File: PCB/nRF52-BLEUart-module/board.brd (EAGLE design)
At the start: 40 x 16 mm, 2 parts, among them J1 USB-A_PTH_MALE, U1 NRF52832

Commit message: PCB update
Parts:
- added C1: 0402, angrypig7-RCL:C0402
- added C10: 2.2uF, angrypig7-RCL:C0603
- added C11, C13, C14, C15, C4, C6: 100nF, angrypig7-RCL:C0402
- added C12: 4.7uF, angrypig7-RCL:C0402
- added C16, C17, C7, C8: 12pF, angrypig7-RCL:C0402
- added C2: 0603, angrypig7-RCL:C0603
- added C3: 0805, angrypig7-RCL:C0805
- added C5: 10uF, angrypig7-RCL:C0603
- added C9: 1uF, angrypig7-RCL:C0402
- added D1: B5819W, angrypig7-Diodes:SOD-123
- added JP1: (no value), angrypig7-Connectors-PinHeads:1X04
- added TC1: TC2030-IDC-NL, angrypig7-Connectors-Programming:TC2030-IDC-NL
- added TP1: TEST-POINT-3, angrypig7-Tests:PAD-3X-RECT-SILK
- added VR1: AP2210K-3.3TRG, angrypig7-IC-Power:SOT-23-5
- added Y1: 32.768kHz, angrypig7-Clocks:CRYSTAL-SMD-3.2X1.5MM
- added Y2: 32MHz_2016, angrypig7-Clocks:CRYSTAL-SMD-2.0X1.6MM
- moved U1 17.7 mm to (37.7, 9.65)
- moved J1 1.28 mm to (3.17, 9.27)
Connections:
- removed net VBUS: J1.VBUS
- new net 3V3: C10.1, C12.1, C14.1, C15.1, TC1.1, TP1.P$2, U1.13, U1.36, U1.48, VR1.5
- new net 5V: C9.1, D1.C, TP1.P$3, VR1.1, VR1.3
- new net N$1: C8.2, U1.2, Y1.P$2
- new net N$2: C4.1, D1.A, J1.VBUS
- new net N$3: C6.1, VR1.4
- new net N$4: C7.2, U1.3, Y1.P$1
- new net N$5: C11.1, U1.1
- new net N$6: U1.30
- new net N$7: C13.1, U1.46
- new net N$8: C17.1, U1.35, Y2.3
- new net N$9: C16.1, U1.34, Y2.1
- new net NRST: TC1.3, U1.24
- new net SWDCLK: TC1.4, U1.25
- new net SWDIO: TC1.2, U1.26
- new net SWO: TC1.6, U1.21
- new net USB_D_N: J1.D-
- new net USB_D_P: J1.D+
- net GND: now also C10.2, C11.2, C12.2, C13.2, C14.2, C15.2, C16.2, C17.2, C4.2, C6.2, C7.1, C8.1, C9.2, J1.SHIELD@0, J1.SHIELD@1, J1.SHIELD@2, J1.SHIELD@3, TC1.5, TP1.P$1, U1.45, VR1.2, Y2.2, Y2.4
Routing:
- added copper zone on layer 1, net GND
- added copper zone on layer 16, net GND
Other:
- board size 40 x 16 mm -> 55 x 18 mm

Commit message: PCB update
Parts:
- added D2: TVS, angrypig7-Diodes:SPT-23-6
- added D3, D4, D5, D6: 0603, angrypig7-Diodes:LED_0603
- added L1: (no value), angrypig7-RCL:R0402
- added R1, R2, R3, R4, R5: 10k, angrypig7-RCL:R0402
- added S1: SPST-3x4mm, angrypig7-Switches:TACTILE_SWITCH_SMD_3.0X4.0MM
- added U2: NRF52832, angrypig7-IC-MCU:QFN40P600X600X90-49T450N
- C1: value 0402 -> 1uF
- C10: value 2.2uF -> 100nF; device angrypig7-RCL:C0603 -> angrypig7-RCL:C0402
- C11, C6: value 100nF -> 12pF
- C12: value 4.7uF -> 100nF
- C13: value 100nF -> 100pF
- C14: value 100nF -> 1uF
- C15: value 100nF -> 0.8pF
- C16: value 12pF -> 0.8pF
- C17: value 12pF -> 100nF
- C2: value 0603 -> 2.2uF
- C3: value 0805 -> 100nF; device angrypig7-RCL:C0805 -> angrypig7-RCL:C0402
- C5: value 10uF -> 4.7uF; device angrypig7-RCL:C0603 -> angrypig7-RCL:C0402
- C9: value 1uF -> 100nF
- JP1: value (none) -> V G Rx Tx; device angrypig7-Connectors-PinHeads:1X04 -> angrypig7-Connectors-PinHeads:1X04/90
- U1: value NRF52832 -> CH340E; device angrypig7-IC-MCU:QFN40P600X600X90-49T450N -> angrypig7-IC:MSOP-10
- Y1: value 32.768kHz -> 32MHz_2016; device angrypig7-Clocks:CRYSTAL-SMD-3.2X1.5MM -> angrypig7-Clocks:CRYSTAL-SMD-2.0X1.6MM
- Y2: value 32MHz_2016 -> 32.768kHz; device angrypig7-Clocks:CRYSTAL-SMD-2.0X1.6MM -> angrypig7-Clocks:CRYSTAL-SMD-3.2X1.5MM
- moved C12 29.6 mm to (7.75, 2.03)
- moved U1 28.3 mm to (10.0, 3.68), turned to 270 degrees
- moved Y2 22.6 mm to (21.3, 11.4)
- moved C17 22.2 mm to (24.4, 4.57), turned to 180 degrees
- moved C6 21.7 mm to (32.4, 14.1), turned to 0 degrees
- moved C4 21.2 mm to (25.8, 13.0), turned to 0 degrees
- moved C9 17.2 mm to (30.2, 13.0), turned to 90 degrees
- moved C14 13.5 mm to (27.2, -5.46), turned to 0 degrees
- moved TC1 13.0 mm to (30.9, 2.54), turned to 180 degrees
- moved C1 12.7 mm to (15.4, 16.9), turned to 180 degrees
- moved C2 12.0 mm to (14.9, 11.2), turned to 180 degrees
- moved C5 11.4 mm to (24.1, 13.2)
- moved C15 11.1 mm to (31.9, 7.37), turned to 270 degrees
- moved C7 10.2 mm to (19.6, 10.3)
- moved C8 10.2 mm to (19.6, 12.6)
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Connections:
- removed net USB_D_N: J1.D-
- removed net USB_D_P: J1.D+
- new net N$10: C13.1, U2.33
- new net N$11: U2.32
- new net N$12: D4.A, R3.1
- new net N$13: D5.A, R4.1
- new net N$14: D6.A, R5.1
- new net RF-1: C15.1, L1.1, U2.30
- new net RF-2: C16.1, L1.2
- new net UART_RX: JP1.4, U1.9
- new net UART_TX: JP1.3, U1.8
- new net USB_N: D2.4, D2.6, J1.D-, U1.2
- new net USB_P: D2.1, D2.3, J1.D+, U1.1
- net 3V3: now also C17.1, C2.1, C5.1, C9.1, JP1.1, R1.2, R2.2, R3.2, R4.2, R5.2, U1.10, U1.7, U2.13, U2.36, U2.48; no longer C10.1, C14.1, C15.1, U1.13, U1.36, U1.48
- net 5V: now also C1.1; no longer C9.1
- net GND: now also C1.2, C2.2, C3.2, C5.2, D2.2, D3.C, JP1.2, S1.1, U1.3, U2.31, U2.45, U2.49, Y1.2, Y1.4; no longer U1.45, Y2.2, Y2.4
- net N$1: now also U2.2, Y2.P$2; no longer U1.2, Y1.P$2
- net N$2: now also D2.5; no longer C4.1
- net N$3: now also C3.1; no longer C6.1
- net N$4: now also U2.3, Y2.P$1; no longer U1.3, Y1.P$1
- net N$5: now also C10.1, U2.1; no longer C11.1, U1.1
- net N$6: now also D3.A, R1.1; no longer U1.30
- net N$7: now also C4.1, U2.46; no longer C13.1, U1.46
- net N$8: now also C6.1, U2.35, Y1.3; no longer C17.1, U1.35, Y2.3
- net N$9: now also C11.1, U2.34, Y1.1; no longer C16.1, U1.34, Y2.1
- net NRST: now also C14.1, R2.1, S1.2, U2.24; no longer U1.24
- net SWDCLK: now also U2.25; no longer U1.25
- net SWDIO: now also U2.26; no longer U1.26
- net SWO: now also U2.21; no longer U1.21
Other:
- board size 55 x 18 mm -> 50 x 18 mm

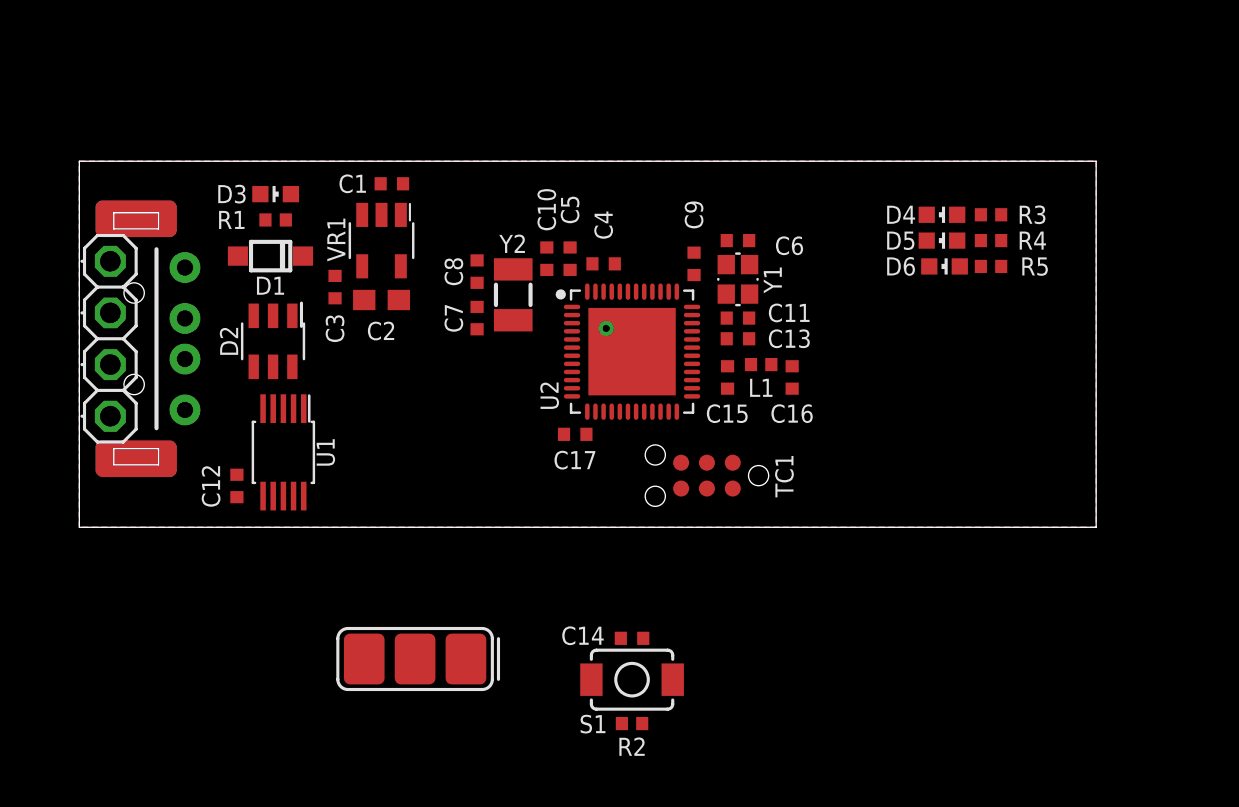
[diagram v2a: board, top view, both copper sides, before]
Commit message: PCB update with inverted F antenna
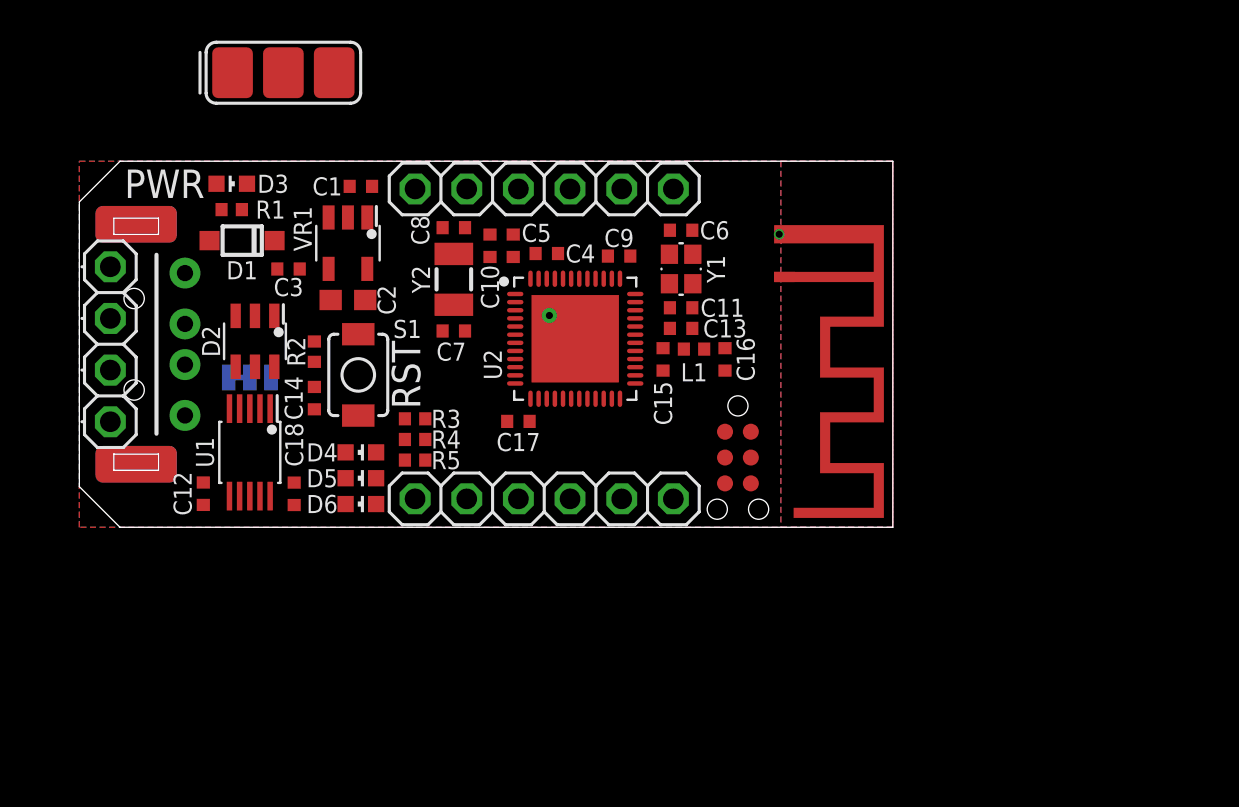
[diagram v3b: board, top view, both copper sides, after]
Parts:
- added C18: 100nF, angrypig7-RCL:C0402
- added JP2: 5V 3V3, angrypig7-Jumpers:SMT-JUMPER_3_1-NC_TRACE_NO-SILK
- added JP3, JP4: (no value), angrypig7-Connectors-PinHeads:1X06
- added U$1: INVERTED_F_2.4GHZ_TI-AN043_L, angrypig7-Antennas:TI-AN043_LEFT
- C15, C16: value 0.8pF -> (none)
- D3: value 0603 -> PWR
- L1: value (none) -> 0R
- moved D6 31.0 mm to (13.8, 1.14)
- moved D4 30.9 mm to (13.8, 3.68)
- moved D5 30.9 mm to (13.8, 2.41)
- moved R3 30.0 mm to (16.5, 5.33)
- moved R4 30.0 mm to (16.5, 4.32)
- moved R5 29.9 mm to (16.5, 3.30)
- moved TP1 29.5 mm to (10.0, 22.4), turned to 0 degrees
- moved R2 24.1 mm to (11.6, 8.64), turned to 90 degrees
- moved S1 20.1 mm to (13.7, 7.49), turned to 270 degrees
- moved C14 19.6 mm to (11.6, 6.35), turned to 270 degrees
- moved C9 3.70 mm to (26.5, 13.3), turned to 180 degrees
- moved C16 3.42 mm to (31.8, 8.26)
- moved L1 3.39 mm to (30.2, 8.76)
- moved C15 3.30 mm to (28.7, 8.26)
- moved Y2 3.02 mm to (18.4, 12.2)
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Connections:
- new net N$15: C12.1, JP2.2, U1.7
- new net N$16: C18.1, U1.10
- net 3V3: now also JP2.3; no longer C12.1, U1.10, U1.7
- net 5V: now also JP2.1
- net GND: now also C18.2, U$1.GND
- net RF-2: now also U$1.RF
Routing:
- added copper zone on layer 1, net GND-CUTOUT
- added copper zone on layer 16, net GND-CUTOUT2
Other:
- board size 50 x 18 mm -> 40 x 18 mm
- board text added: "RST"

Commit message: artwork partially done, layout update
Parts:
- added C19: TP, angrypig7-RCL:C0603
- JP1: value V G Rx Tx -> V G Tx Rx
- JP3, JP4: device angrypig7-Connectors-PinHeads:1X06 -> angrypig7-Connectors-PinHeads:1X05-NOSILK
- moved TP1 6.26 mm to (10.7, 16.1), flipped to the bottom
- moved JP2 5.68 mm to (10.9, 12.4), turned to 270 degrees
- moved C11 3.95 mm to (31.8, 14.1), turned to 270 degrees
- moved C16 3.91 mm to (30.9, 12.1), turned to 180 degrees
- moved C15 3.27 mm to (31.9, 9.02), turned to 0 degrees
- moved TC1 2.17 mm to (30.2, 3.17)
- moved L1 2.11 mm to (31.4, 10.5), turned to 90 degrees
- moved C6 1.73 mm to (27.9, 14.1), turned to 90 degrees
- moved Y1 1.42 mm to (29.8, 14.1), turned to 180 degrees
- moved JP1 1.40 mm to (2.92, 9.00)
- moved JP4 1.29 mm to (21.6, 1.20)
- moved JP3 1.28 mm to (21.6, 16.8)
- moved C13 1.09 mm to (29.2, 10.8), turned to 90 degrees
- moved U$1 0.88 mm to (33.3, 14.7)
- moved C9 0.85 mm to (26.9, 14.1), turned to 90 degrees
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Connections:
- net N$2 renamed USB_IN
- removed net N$15: C12.1, JP2.2, U1.7
- new net VCCIO: C12.1, JP1.1, JP2.2, U1.7
- net 3V3: no longer JP1.1
- net GND: now also C19.2
- net RF-1: now also C19.1
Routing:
- net VCCIO: track 0.00 -> 23.1 mm, vias 0 -> 1
- net 3V3: track 0.00 -> 22.9 mm, vias 0 -> 3
- net UART_RX: track 0.00 -> 15.5 mm, vias 0 -> 1
- net 5V: track 0.00 -> 13.2 mm, vias 0 -> 1
- net USB_IN: track 0.00 -> 12.2 mm, vias 0 -> 2
- net UART_TX: track 0.00 -> 12.0 mm, vias 0 -> 2
- net USB_P: track 0.00 -> 11.3 mm
- net USB_N: track 0.00 -> 8.85 mm
- net N$1: track 0.00 -> 5.36 mm
- net N$4: track 0.00 -> 4.58 mm
- net NRST: track 0.00 -> 4.10 mm
- net N$5: track 0.00 -> 2.63 mm
- net N$16: track 0.00 -> 1.71 mm
- net N$3: track 0.00 -> 1.58 mm
- net N$7: track 0.00 -> 1.47 mm
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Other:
- board size 40 x 18 mm -> 39 x 18 mm

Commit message: finished PCB artwork
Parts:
- removed C19: TP, angrypig7-RCL:C0603
- JP2: value 5V 3V3 -> 3V3 5V
- U$1: value INVERTED_F_2.4GHZ_TI-AN043_L -> ANT
- moved TC1 1.14 mm to (30.7, 4.19)
- moved C13 0.38 mm to (29.2, 10.4)
- moved C15 0.38 mm to (31.5, 9.02)
- moved L1 0.38 mm to (31.0, 10.5)
- moved C16 0.25 mm to (30.6, 12.1)
- moved D4 0.18 mm to (13.8, 3.94)
- moved D5 0.18 mm to (13.8, 2.67)
- moved D6 0.18 mm to (13.8, 1.40)
- moved C7 0.13 mm to (18.3, 9.27), turned to 0 degrees
- moved C8 0.13 mm to (18.3, 14.4), turned to 0 degrees
- moved Y2 0.13 mm to (18.3, 11.8)
- turned JP2 to 90 degrees
- turned R3 to 180 degrees
- turned R4 to 180 degrees
- turned R5 to 180 degrees
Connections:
- removed net N$13: D5.A, R4.1
- new net LED1: R3.1, U2.17
- new net LED2: R4.1, U2.18
- new net LED3: R5.1, U2.19
- new net N$2: D4.A, R3.2
- new net P0.02: JP4.2, U2.4
- new net P0.03: JP4.3, U2.5
- new net P0.04: JP4.4, U2.6
- new net P0.05: JP4.5, U2.7
- new net P0.28: JP3.5, U2.40
- new net P0.29: JP3.4, U2.41
- new net P0.30: JP3.3, U2.42
- new net P0.31: JP3.2, U2.43
- net 3V3: now also JP2.1, JP3.1; no longer JP2.3, R3.2, R4.2, R5.2
- net 5V: now also JP2.3; no longer JP2.1
- net GND: now also D4.C, D5.C, D6.C, JP4.1; no longer C19.2
- net N$12: now also D5.A, R4.2; no longer D4.A, R3.1
- net N$14: now also R5.2; no longer R5.1
- net RF-1: no longer C19.1
- net UART_RX: now also U1.8, U2.10; no longer U1.9
- net UART_TX: now also U1.9, U2.8; no longer U1.8
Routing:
- net 3V3: track 22.9 -> 64.2 mm, vias 3 -> 8
- net NRST: track 4.10 -> 24.7 mm, vias 0 -> 2
- net UART_TX: track 12.0 -> 28.3 mm, vias 2 -> 4
- net UART_RX: track 15.5 -> 29.8 mm, vias 1 -> 3
- net P0.05: track 0.00 -> 14.1 mm
- net P0.04: track 0.00 -> 12.7 mm
- net LED3: track 0.00 -> 12.3 mm, vias 0 -> 2
- net LED2: track 0.00 -> 11.6 mm, vias 0 -> 2
- net P0.03: track 0.00 -> 11.4 mm
- net P0.02: track 0.00 -> 11.1 mm
- net LED1: track 0.00 -> 11.1 mm, vias 0 -> 2
- net P0.31: track 0.00 -> 8.80 mm
- net SWO: track 0.00 -> 8.41 mm, vias 0 -> 2
- net N$9: track 0.00 -> 7.32 mm
- net P0.30: track 0.00 -> 6.70 mm
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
